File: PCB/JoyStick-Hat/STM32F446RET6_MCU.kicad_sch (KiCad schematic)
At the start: 1 part, among them U1 STM32F446RET6

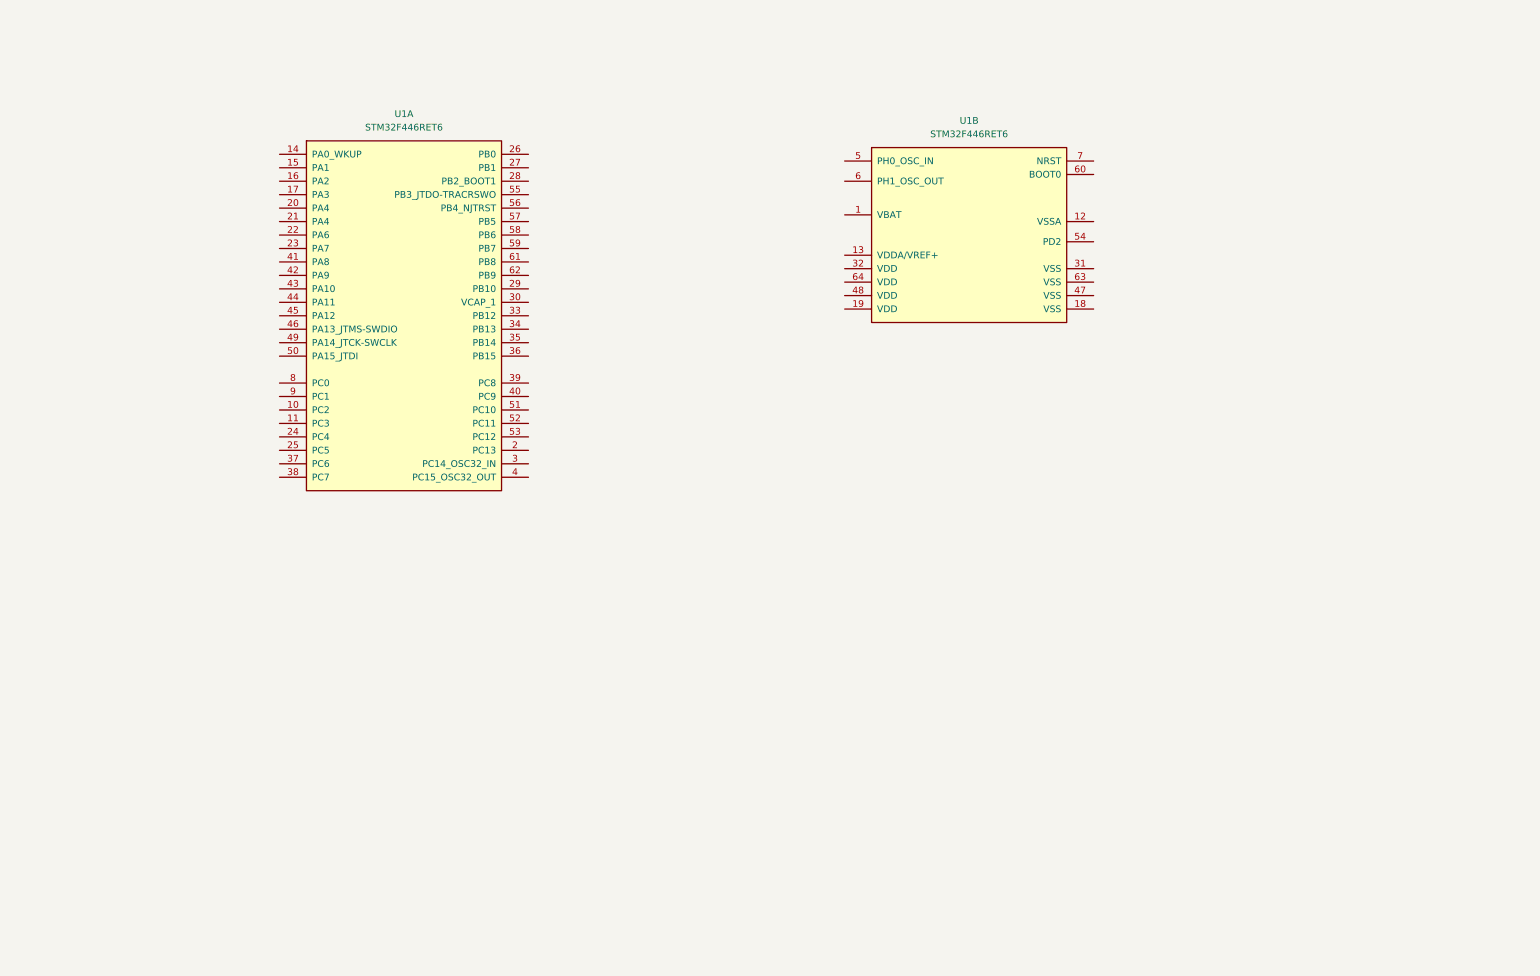
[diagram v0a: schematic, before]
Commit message: MCU
MCU schematic added and 90% complete
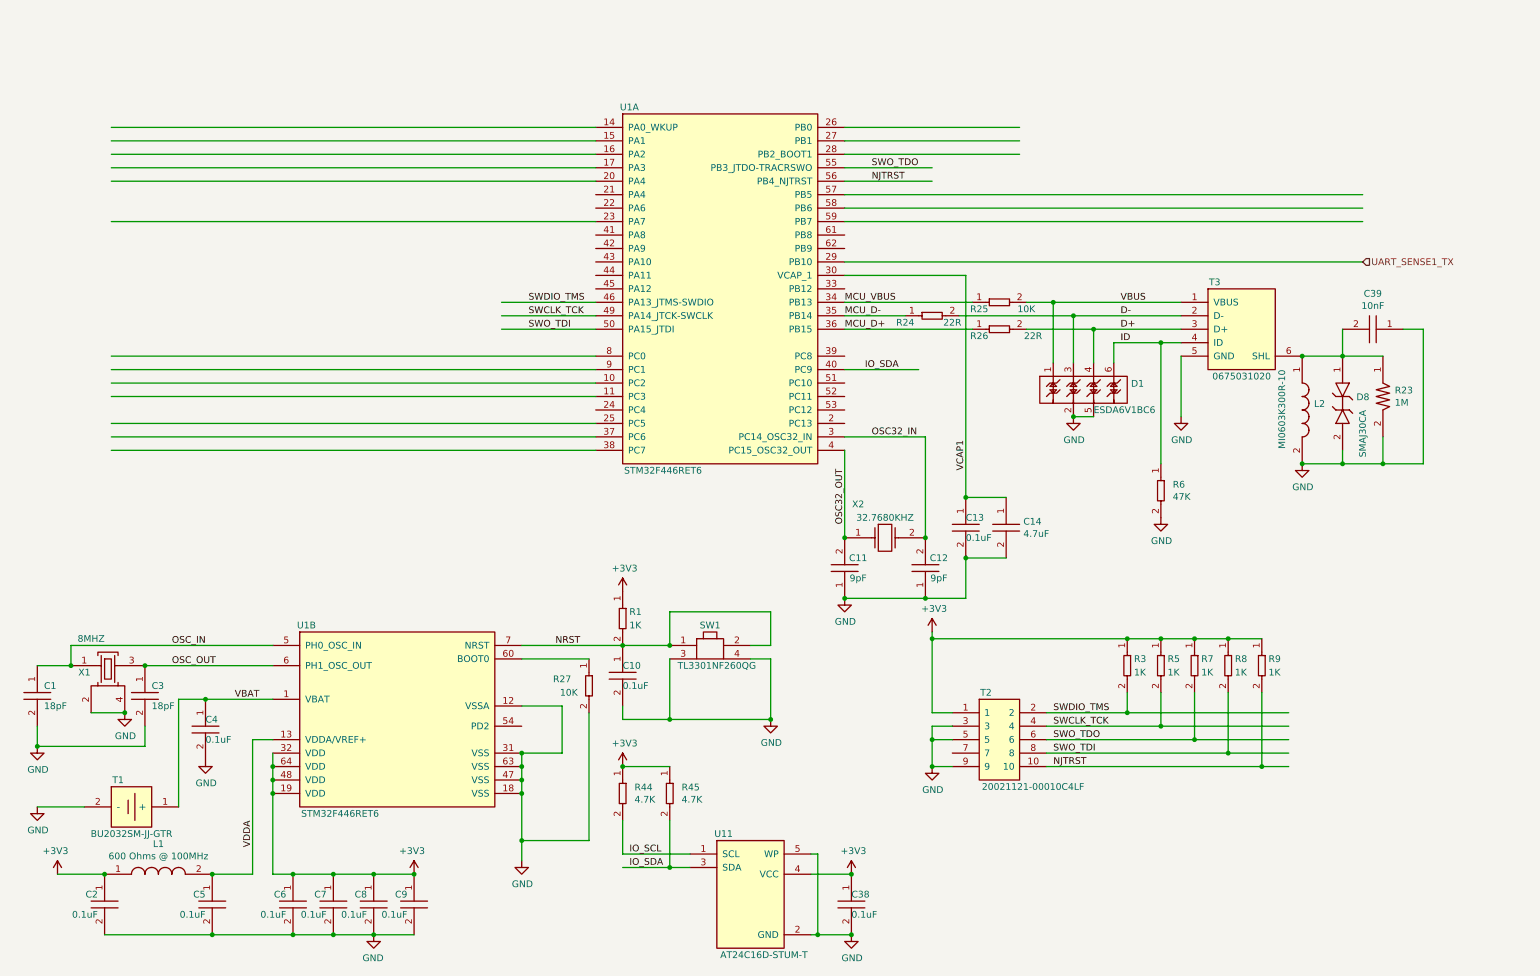
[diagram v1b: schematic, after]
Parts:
- added C1, C3: GCM1555C1H180GA16D, growbox-KiCAD-Capacitors:C0402, symbol AVR-KiCAD-Lib-Capacitors:GCM1555C1H180GA16D
- added C10, C13, C2, C38, C4, C5, C6, C7, C8, C9: C0402C104K9PACTU, AVR-KiCAD-Lib-Resistors:R0402, symbol AVR-KiCAD-Lib-Capacitors:C0402C104K9PACTU
- added C11, C12: CL05C090CB5NNNC, growbox-KiCAD-Capacitors:C0402, symbol AVR-KiCAD-Lib-Capacitors:CL05C090CB5NNNC
- added C14: GRM155R60J475ME47D, growbox-KiCAD-Capacitors:C0402, symbol AVR-KiCAD-Lib-Capacitors:GRM155R60J475ME47D
- added C39: C0603X103K1RAC3316, AVR-KiCAD-Lib-Capacitors:C0603, symbol AVR-KiCAD-Lib-Capacitors:C0603X103K1RAC3316
- added D1: ESDA6V1BC6, AVR-KiCAD-Lib-ICs:SOT-23-6_Handsoldering, symbol AVR-KiCAD-Lib-Diodes:ESDA6V1BC6
- added D8: SMAJ30CA, AVR-KiCAD-Lib-Diodes:SMAJ30CA, symbol AVR-KiCAD-Lib-Diodes:SMAJ30CA
- added L1: BLM15HG601SN1D, AVR-KiCAD-Lib-Inductors:BLM15HG601SN1D, symbol AVR-KiCAD-Lib-Inductors:BLM15HG601SN1D
- added L2: MI0603K300R-10, AVR-KiCAD-Lib-Inductors:MI0603K300R-10, symbol AVR-KiCAD-Lib-Inductors:MI0603K300R-10
- added R1, R3, R5, R7, R8, R9: RC0402FR-071KL, AVR-KiCAD-Lib-Resistors:R0402, symbol AVR-KiCAD-Lib-Resistors:RC0402FR-071KL
- added R23: RC1206FR-071ML, AVR-KiCAD-Lib-Resistors:R1206, symbol AVR-KiCAD-Lib-Resistors:RC1206FR-071ML
- added R24, R26: RC0402FR-0722RL, AVR-KiCAD-Lib-Resistors:R0402, symbol AVR-KiCAD-Lib-Resistors:RC0402FR-0722RL
- added R25, R27: RC0402FR-0710KL, AVR-KiCAD-Lib-Resistors:R0402, symbol AVR-KiCAD-Lib-Resistors:RC0402FR-0710KL
- added R44, R45: RC0402FR-074K7L, AVR-KiCAD-Lib-Resistors:R0402, symbol AVR-KiCAD-Lib-Resistors:RC0402FR-074K7L
- added R6: RC0603FR-0747KL, AVR-KiCAD-Lib-Resistors:R0603, symbol AVR-KiCAD-Lib-Resistors:RC0603FR-0747KL
- added SW1: TL3301NF260QG, AVR-KiCAD-Lib-Mech-Switches:TL3301NF260QG, symbol AVR-KiCAD-Lib-Mech-Switches:TL3301NF260QG
- added T1: BU2032SM-JJ-GTR, AVR-KiCAD-Lib-Battery-Holders:BU2032SM-JJ-GTR, symbol AVR-KiCAD-Lib-Battery-Holders:BU2032SM-JJ-GTR
- added T2: 20021121-00010C4LF, AVR-KiCAD-Lib-Connectors:20021121-00010C4LF, symbol AVR-KiCAD-Lib-Connectors:20021121-00010C4LF
- added T3: 0675031020, AVR-KiCAD-Lib-Connectors:USB_Mini-B, symbol AVR-KiCAD-Lib-Connectors:0675031020
- added U11: AT24C16D-STUM-T, AVR-KiCAD-Lib-ICs:SOT-23-5, symbol AVR-KiCAD-Lib-ICs:AT24C16D-STUM-T
- added X1: ABM3B-8.000MHZ-B2-T, AVR-KiCAD-Lib-Oscillators:ABM3B8.000MHZB2T, symbol AVR-KiCAD-Lib-Oscillators-Clocks:ABM3B-8.000MHZ-B2-T
- added X2: ABS07-32.768KHZ-9-T, AVR-KiCAD-Lib-Oscillators:ABS07-32.768KHZ-9-T, symbol AVR-KiCAD-Lib-Oscillators-Clocks:ABS07-32.768KHZ-9-T
- U1: Voltage 1.7V ~{} 3.6V -> 1.7V ~ 3.6V
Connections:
- net UART_SENSE1_TX: now reaches U1.29 (PB10)
- net OSC32_IN: now reaches U1.3 (PC14_OSC32_IN)
- net OSC32_IN: now also C12.2, X2.2
- net VCAP1: now reaches U1.30 (VCAP_1)
- net VCAP1: now also C13.1, C14.1
- net MCU_VBUS: now reaches U1.34 (PB13)
- net MCU_VBUS: now also R25.1
- net MCU_D-: now reaches U1.35 (PB14)
- net MCU_D-: now also R24.1
- net MCU_D+: now reaches U1.36 (PB15)
- net MCU_D+: now also R26.1
- net OSC32_OUT: now reaches U1.4 (PC15_OSC32_OUT)
- net OSC32_OUT: now also C11.2, X2.1
- net IO_SDA: now reaches U1.40 (PC9)
- net IO_SDA: now also R45.2, U11.3 (SDA)
- net SWDIO_TMS: now reaches U1.46 (PA13_JTMS-SWDIO)
- net SWDIO_TMS: now also R3.2, T2.2
- net SWCLK_TCK: now reaches U1.49 (PA14_JTCK-SWCLK)
- net SWCLK_TCK: now also R5.2, T2.4
- net SWO_TDI: now reaches U1.50 (PA15_JTDI)
- net SWO_TDI: now also R8.2, T2.8
- net SWO_TDO: now reaches U1.55 (PB3_JTDO-TRACRSWO)
- net SWO_TDO: now also R7.2, T2.6
- net NJTRST: now reaches U1.56 (PB4_NJTRST)
- net NJTRST: now also R9.2, T2.10
- net VBAT: now reaches U1.1 (VBAT)
- net VBAT: now also C4.1, T1.1 (+)
- net GND: now reaches U1.12 (VSSA)
- net GND: now also U1.18 (VSS), U1.31 (VSS), U1.47 (VSS), U1.63 (VSS), C1.2, C10.2, C11.1, C12.1, C13.2, C14.2, C2.2, C3.2, C38.2, C39.1, C4.2, C5.2, C6.2, C7.2, C8.2, C9.2, D1.2, D1.5, D8.2, L2.2, R23.2, R27.2, R6.2, SW1.3, SW1.4, T1.2 (-), T2.3, T2.5, T2.9, T3.5 (GND), U11.2 (GND), U11.5 (WP), X1.2, X1.4
- net VDDA: now reaches U1.13 (VDDA/VREF+)
- net VDDA: now also C5.1, L1.2
- net +3V3: now reaches U1.19 (VDD)
- net +3V3: now also U1.32 (VDD), U1.48 (VDD), U1.64 (VDD), C2.1, C38.1, C6.1, C7.1, C8.1, C9.1, L1.1, R1.1, R3.1, R44.1, R45.1, R5.1, R7.1, R8.1, R9.1, T2.1, U11.4 (VCC)
- net OSC_IN: now reaches U1.5 (PH0_OSC_IN)
- net OSC_IN: now also C1.1, X1.1
- net OSC_OUT: now reaches U1.6 (PH1_OSC_OUT)
- net OSC_OUT: now also C3.1, X1.3
- net at U1.60 (BOOT0): now also R27.1
- net NRST: now reaches U1.7 (NRST)
- net NRST: now also C10.1, R1.2, SW1.1, SW1.2
- new net: C39.2, D8.1, L2.1, R23.1, T3.6 (SHL)
- new net D+: D1.4, R26.2, T3.3 (D+)
- new net D-: D1.3, R24.2, T3.2 (D-)
- new net ID: D1.6, R6.1, T3.4 (ID)
- new net IO_SCL: R44.2, U11.1 (SCL)
- new net VBUS: D1.1, R25.2, T3.1 (VBUS)

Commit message: Power and LED Driver
Power Supply Schematic sketched out using Pololu power regulator modules to hasten design. LED drivers replaced with ones that have 24 ouputs so we can use 20 unit bar graph LEDs and have 8 extra channels for other onboard LEDs
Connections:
- net UART_SENSE1_TX: no longer names the net of U1.29 (PB10)
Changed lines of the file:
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@@
     (effects (font (size 1.27 1.27)) (justify left bottom))
   )
-  (hierarchical_label "UART_SENSE1_TX" (shape input) (at 266.7 64.77 0) (fields_autoplaced)
+  (hierarchical_label "ST_RPI_UART_CTS" (shape output) (at 34.29 29.21 0) (fields_autoplaced)
     (effects (font (size 1.27 1.27)) (justify left))
   )
+  (hierarchical_label "ST_RPI_UART_TX" (shape output) (at 34.29 26.67 0) (fields_autoplaced)
+    (effects (font (size 1.27 1.27)) (justify left))
+  )
+  (hierarchical_label "ST_RPI_UART_RX" (shape input) (at 34.29 24.13 0) (fields_autoplaced)
+    (effects (font (size 1.27 1.27)) (justify left))
+  )
+  (hierarchical_label "ST_RPI_UART_RTS" (shape input) (at 34.29 21.59 0) (fields_autoplaced)
+    (effects (font (size 1.27 1.27)) (justify left))
+  )

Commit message: LED drivers and Joystick
Finished LED driver scheamtics, corrected some problems with symbols. added conenctors for joystick and buttons, connected RPI pins to MCU
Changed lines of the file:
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@@
     (effects (font (size 1.27 1.27)) (justify left))
+  )
+  (hierarchical_label "LED_DRIVER_SCLK" (shape input) (at 57.15 66.04 180) (fields_autoplaced)
+    (effects (font (size 1.27 1.27)) (justify right))
   )
   (hierarchical_label "ST_RPI_UART_RX" (shape input) (at 34.29 24.13 0) (fields_autoplaced)
@@
     (effects (font (size 1.27 1.27)) (justify left))
   )
+  (hierarchical_label "LED_DRIVER_MOSI" (shape input) (at 57.15 68.58 180) (fields_autoplaced)
+    (effects (font (size 1.27 1.27)) (justify right))
+  )
+  (hierarchical_label "LED_DRIVER_SOUT" (shape input) (at 57.15 71.12 180) (fields_autoplaced)
+    (effects (font (size 1.27 1.27)) (justify right))
+  )
+  (hierarchical_label "LED_DRIVER_XLAT" (shape input) (at 58.42 73.66 180) (fields_autoplaced)
+    (effects (font (size 1.27 1.27)) (justify right))
+  )
+  (hierarchical_label "LED_DRIVER_BLANK" (shape input) (at 57.15 63.5 180) (fields_autoplaced)
+    (effects (font (size 1.27 1.27)) (justify right))
+  )
   (symbol (lib_id "AVR-KiCAD-Lib-ICs:STM32F446RET6") (at 127 36.83 0) (unit 1)

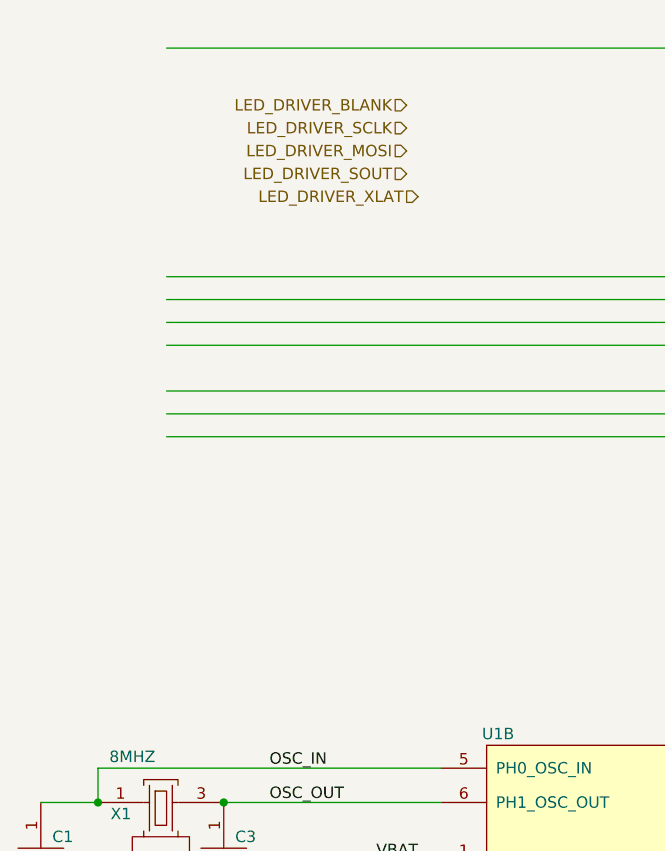
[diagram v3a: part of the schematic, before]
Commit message: Sheet Conenctivity and RS485
Added more sheet entries throughuot the project connecting different subsystems to the main MCU schematic. Also added  new sheet for the RS485 interface for communicating with the motor control board.
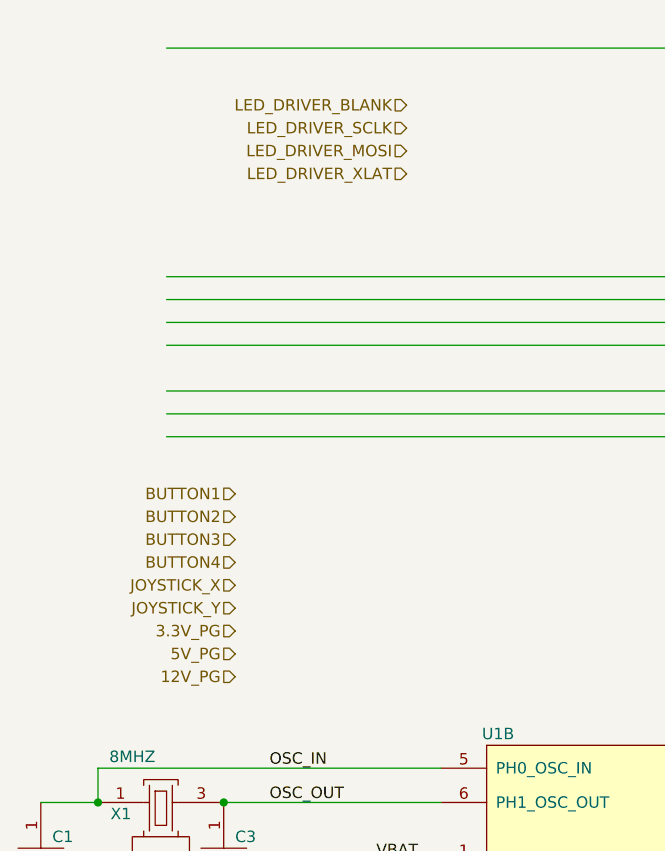
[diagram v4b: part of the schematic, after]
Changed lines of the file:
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@@
     (effects (font (size 1.27 1.27)) (justify left))
+  )
+  (hierarchical_label "BUTTON4" (shape input) (at 38.1 114.3 180) (fields_autoplaced)
+    (effects (font (size 1.27 1.27)) (justify right))
   )
   (hierarchical_label "ST_RPI_UART_TX" (shape output) (at 34.29 26.67 0) (fields_autoplaced)
@@
   )
   (hierarchical_label "LED_DRIVER_SCLK" (shape input) (at 57.15 66.04 180) (fields_autoplaced)
+    (effects (font (size 1.27 1.27)) (justify right))
+  )
+  (hierarchical_label "JOYSTICK_X" (shape input) (at 38.1 116.84 180) (fields_autoplaced)
     (effects (font (size 1.27 1.27)) (justify right))
   )
@@
     (effects (font (size 1.27 1.27)) (justify left))
   )
+  (hierarchical_label "BUTTON1" (shape input) (at 38.1 106.68 180) (fields_autoplaced)
+    (effects (font (size 1.27 1.27)) (justify right))
+  )
   (hierarchical_label "LED_DRIVER_MOSI" (shape input) (at 57.15 68.58 180) (fields_autoplaced)
     (effects (font (size 1.27 1.27)) (justify right))
   )
-  (hierarchical_label "LED_DRIVER_SOUT" (shape input) (at 57.15 71.12 180) (fields_autoplaced)
+  (hierarchical_label "LED_DRIVER_XLAT" (shape input) (at 57.15 71.12 180) (fields_autoplaced)
     (effects (font (size 1.27 1.27)) (justify right))
   )
-  (hierarchical_label "LED_DRIVER_XLAT" (shape input) (at 58.42 73.66 180) (fields_autoplaced)
+  (hierarchical_label "3.3V_PG" (shape input) (at 38.1 121.92 180) (fields_autoplaced)
+    (effects (font (size 1.27 1.27)) (justify right))
+  )
+  (hierarchical_label "5V_PG" (shape input) (at 38.1 124.46 180) (fields_autoplaced)
     (effects (font (size 1.27 1.27)) (justify right))
   )
@@
     (effects (font (size 1.27 1.27)) (justify right))
   )
+  (hierarchical_label "BUTTON3" (shape input) (at 38.1 111.76 180) (fields_autoplaced)
+    (effects (font (size 1.27 1.27)) (justify right))
+  )
+  (hierarchical_label "12V_PG" (shape input) (at 38.1 127 180) (fields_autoplaced)
+    (effects (font (size 1.27 1.27)) (justify right))
+  )
+  (hierarchical_label "JOYSTICK_Y" (shape input) (at 38.1 119.38 180) (fields_autoplaced)
+    (effects (font (size 1.27 1.27)) (justify right))
+  )
+  (hierarchical_label "BUTTON2" (shape input) (at 38.1 109.22 180) (fields_autoplaced)
+    (effects (font (size 1.27 1.27)) (justify right))
+  )
